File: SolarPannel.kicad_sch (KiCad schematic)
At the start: 10 parts, among them U1 ADS1115IDGS

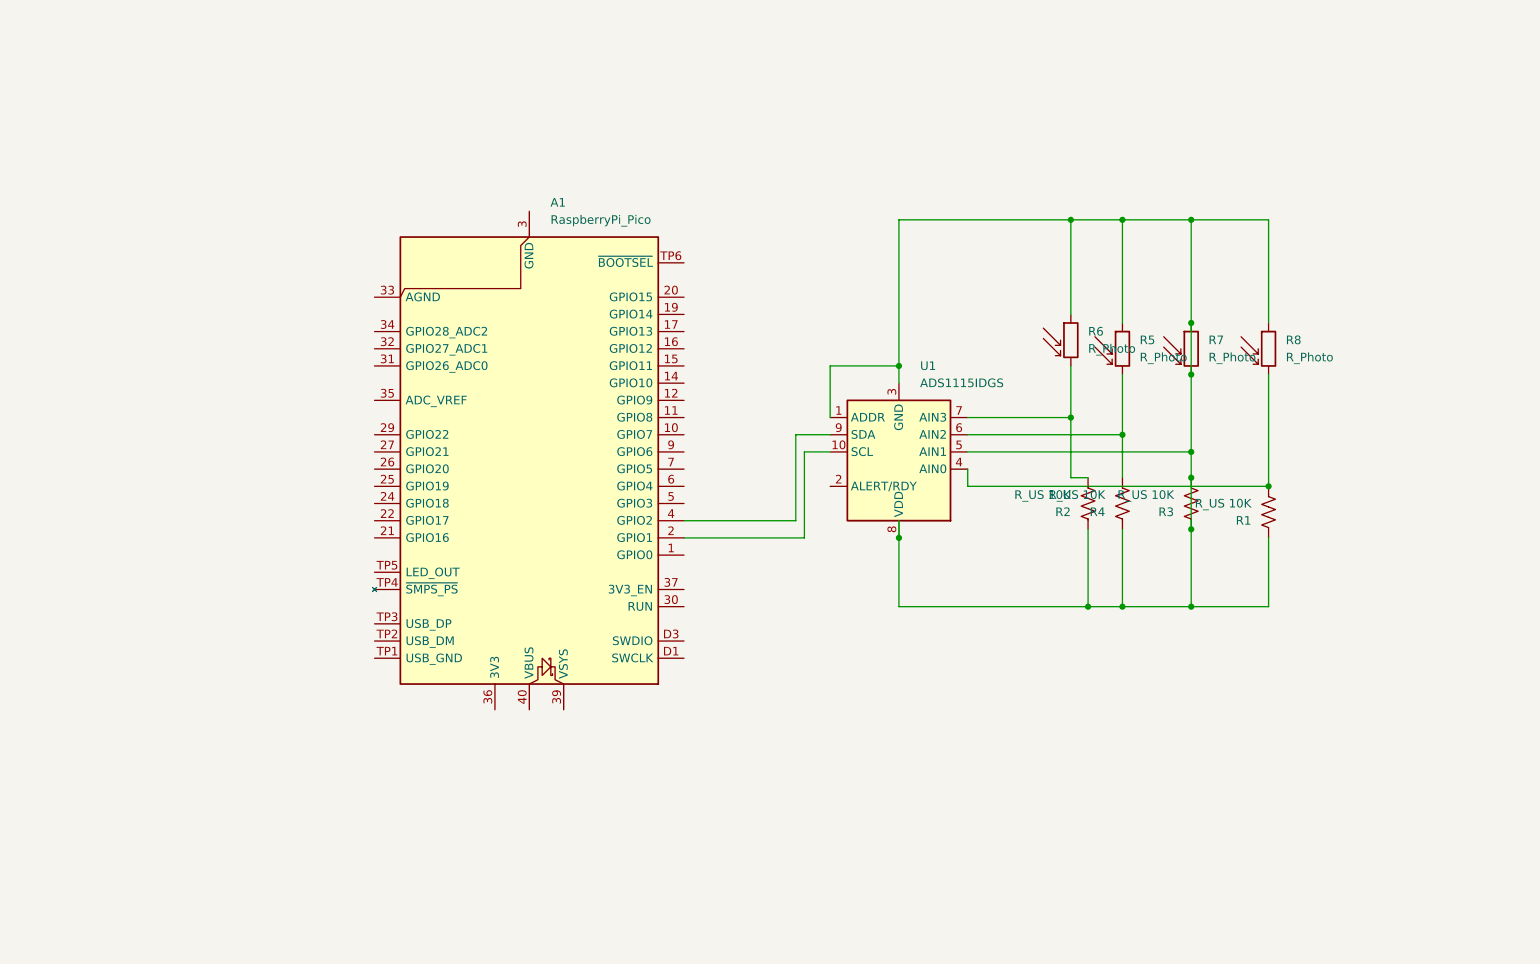
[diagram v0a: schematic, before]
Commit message: Added the Stepper motors, Gotta do some bug fixing later
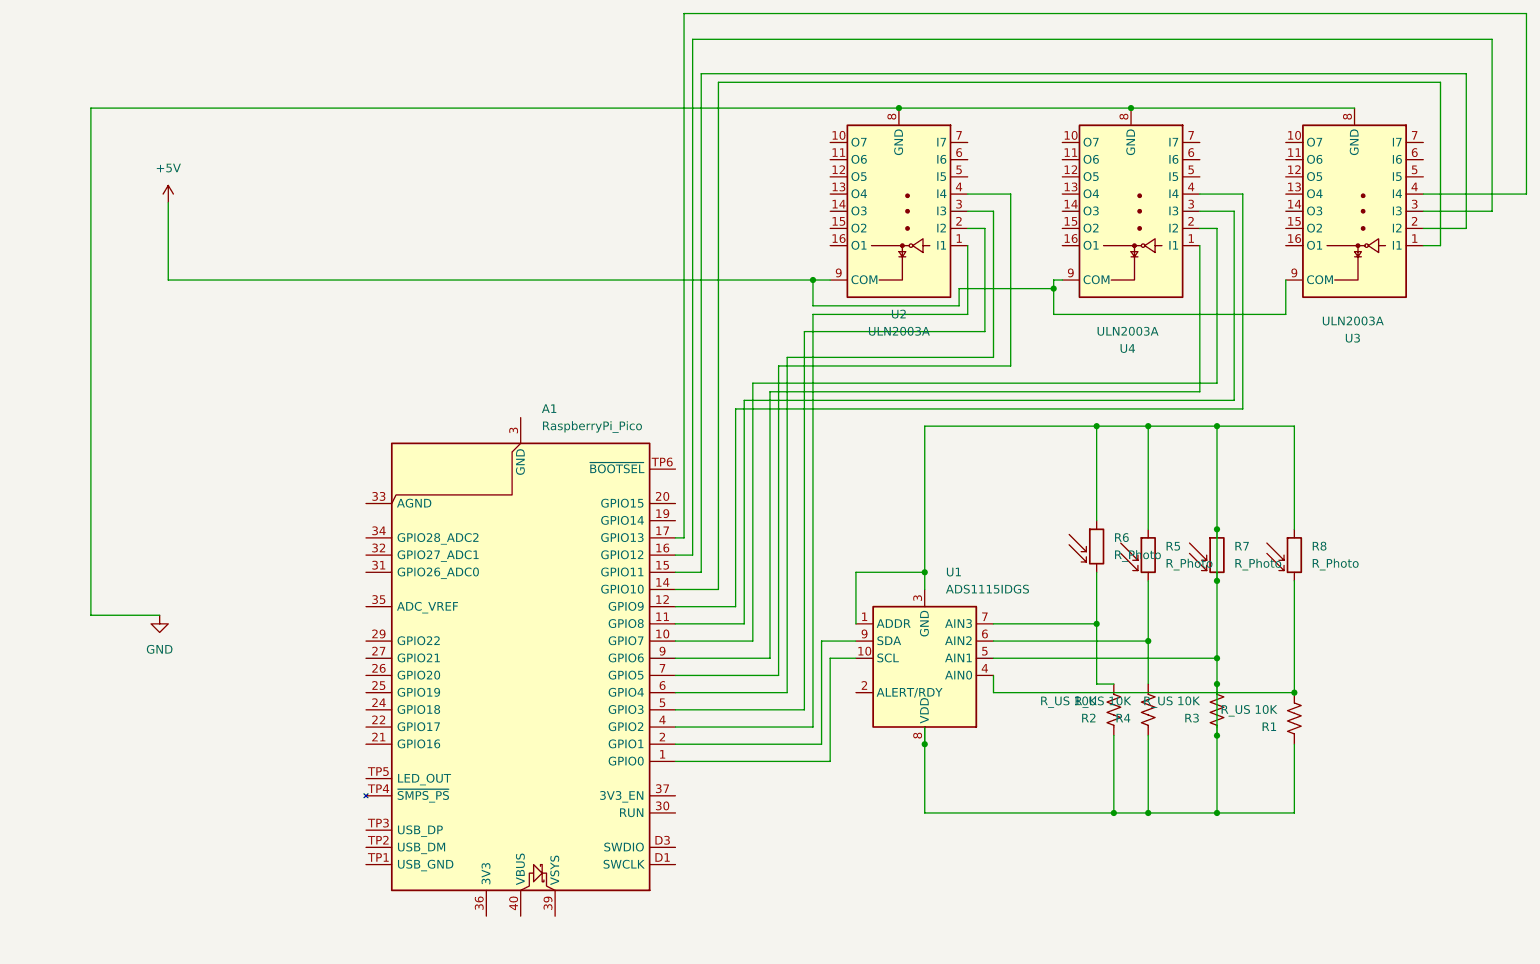
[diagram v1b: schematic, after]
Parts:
- added U2, U3, U4: ULN2003A, symbol Transistor_Array:ULN2003A
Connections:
- net at U1.10 (SCL): now also A1.1 (GPIO0); no longer A1.2 (GPIO1)
- net at A1.4 (GPIO2): now also U2.1 (I1); no longer U1.9 (SDA)
- net at A1.10 (GPIO7): now also U4.2 (I2)
- net at A1.11 (GPIO8): now also U4.3 (I3)
- net at A1.12 (GPIO9): now also U4.4 (I4)
- net at A1.14 (GPIO10): now also U3.1 (I1)
- net at A1.15 (GPIO11): now also U3.2 (I2)
- net at A1.16 (GPIO12): now also U3.3 (I3)
- net at A1.17 (GPIO13): now also U3.4 (I4)
- net at A1.5 (GPIO3): now also U2.2 (I2)
- net at A1.6 (GPIO4): now also U2.3 (I3)
- net at A1.7 (GPIO5): now also U2.4 (I4)
- net at A1.9 (GPIO6): now also U4.1 (I1)
- new net: A1.2 (GPIO1), U1.9 (SDA)
- new net +5V: U2.9 (COM), U3.9 (COM), U4.9 (COM)
- new net GND: U2.8 (GND), U3.8 (GND), U4.8 (GND)
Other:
- moved on the sheet: A1, R1, R2, R3, R4, R5, R6, R7, R8, U1

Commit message: Included the INA chip (Complete Version 1.0)
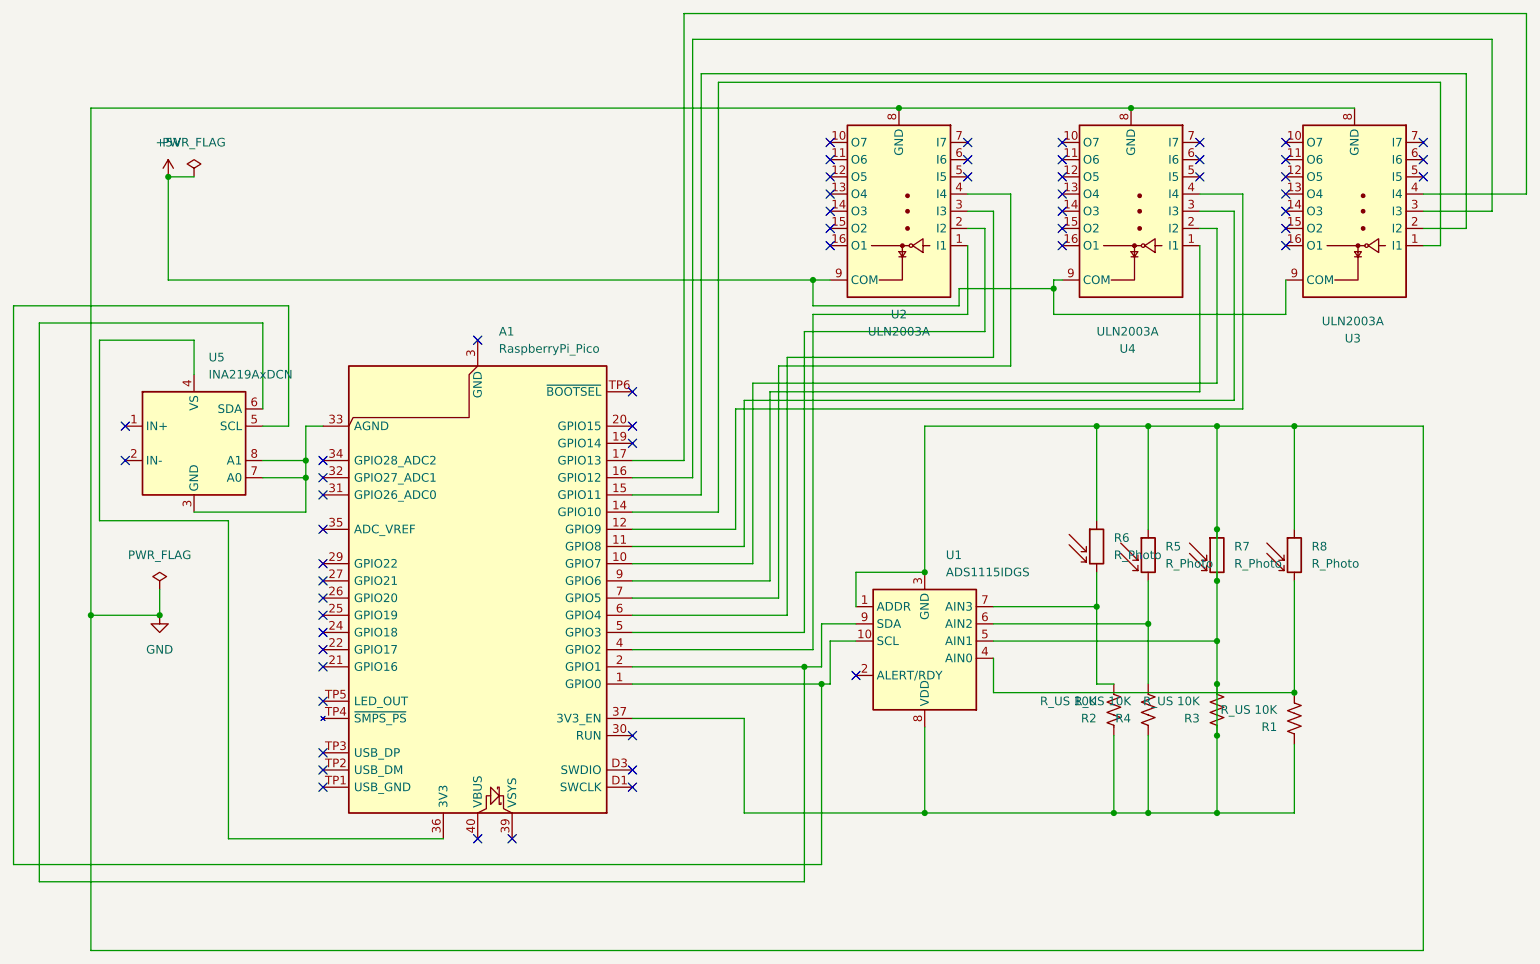
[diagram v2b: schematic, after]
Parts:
- added U5: INA219AxDCN, Package_TO_SOT_SMD:SOT-23-8, symbol Sensor_Energy:INA219AxDCN
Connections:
- net GND: now also A1.37 (3V3_EN), R1.1, R2.1, R3.1, R3.2, R4.1, R5.1, R6.1, R7.1, R7.2, R8.1, U1.1 (ADDR), U1.3 (GND), U1.5 (AIN1), U1.8 (VDD)
- net at A1.1 (GPIO0), U1.10 (SCL): now also U5.5 (SCL)
- net at A1.2 (GPIO1), U1.9 (SDA): now also U5.6 (SDA)
- net at A1.33 (AGND): now also U5.3 (GND), U5.7 (A0), U5.8 (A1)
- net at A1.36 (3V3): now also U5.4 (VS)
- no-connect marks 0 -> 57
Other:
- moved on the sheet: A1, U1
